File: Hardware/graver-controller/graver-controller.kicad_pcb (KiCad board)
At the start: 2 copper layers, 95 x 70 mm, 117 parts, among them J101 Power in 2p, J201 Handpiece pads 1x4, J301 USB-C, J302 SWD, J401 LCD pads 1x7, J402 Pedal pads 1x4, J403 Encoder pads 1x4, Q101 DMP6023LE, Q201 IRLR3410, Q202 SI2309CDS, Q203 BSS123, SW301 BOOT0, SW302 RESET, U101 LM5164DDAR, U102 AP2112K-3.3, U201 UCC27517DBVR, U202 TLV9062IDR, U301 STM32F411CEU6, U302 USBLC6-2SC6, U401 PESD5V0S2BT, Y301 25MHz 10pF

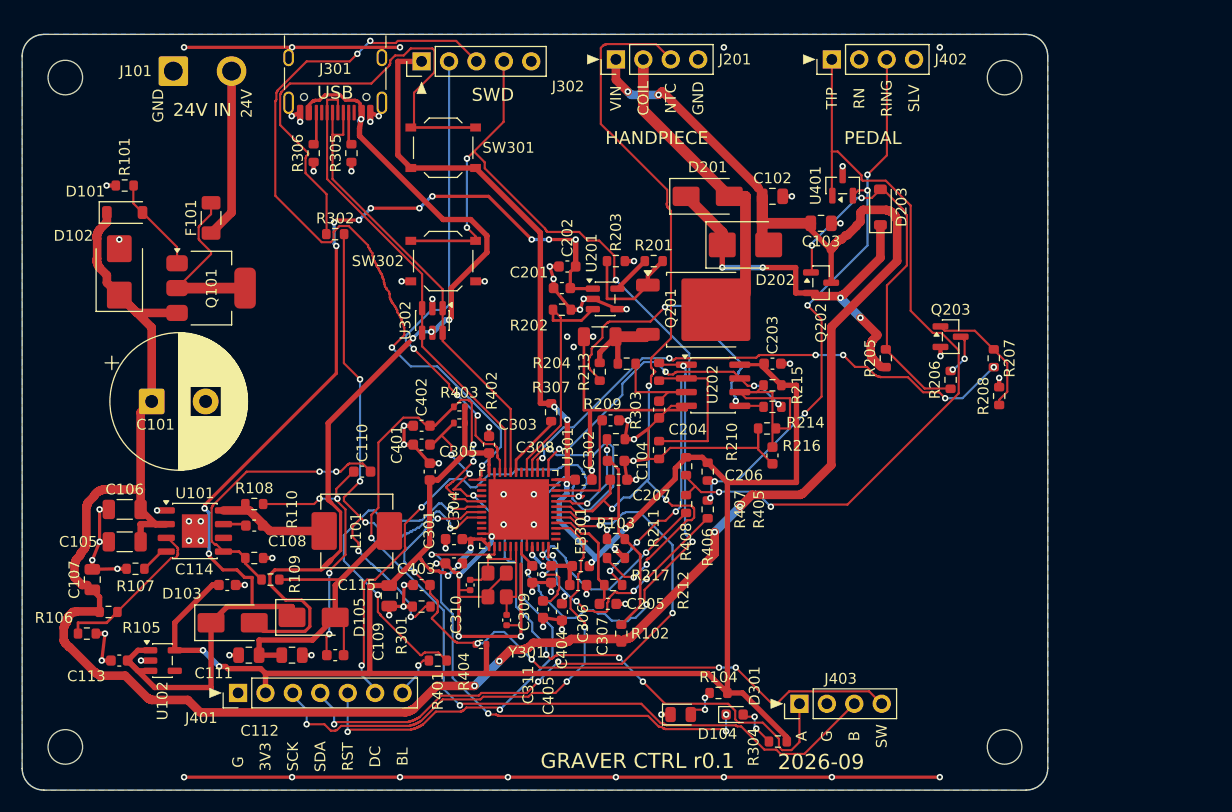
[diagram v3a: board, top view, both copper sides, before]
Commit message: pcb: ADR 0005 stage 1 - 4-layer board, rules, placement with pcbkit
New board from the netlist with pcbkit mkboard: 85 x 60 mm (the ADR 0005
ceiling), JLC04161H-7628 stackup, In1 = GND plane, In2 = +3V3 plane. Net
classes and board rules per ADR 0005 Decision 3 in the .kicad_pro, width
floors in the .kicad_dru, all of it driven from pcbkit.toml.

tools/pcb5/place.py places all 117 parts in bands (power left, MCU centre,
driver right, pad rows on the rear and front edges), adds the M3 and crystal
keepouts, an L-shaped 25 x 20 mm ADR 0004 boost reserve at the front left,
the inner plane zones and the QFN EP vias, and prints the ADR 0003 distance
checks (all PASS). USB-C mouth flush with the rear edge, straight 10.6 mm
run to the MCU for the 0.25/0.15 pair.

tools/pcb5/check.py is the acceptance checker for the component spec
(via and width sets, per-net floors, inner layers track-free, In1 under
USB/crystal/analog, USB skew and vias, placement distances, DRC summary);
postroute.py, render.sh and build.sh are the rest of the pipeline.
tools/pcb/ (ADR 0003 pipeline) stays reachable at tag pcb-pre-pcbkit.
output/pcb/*.png and drc.rpt are no longer ignored (ADR 0005 acceptance).
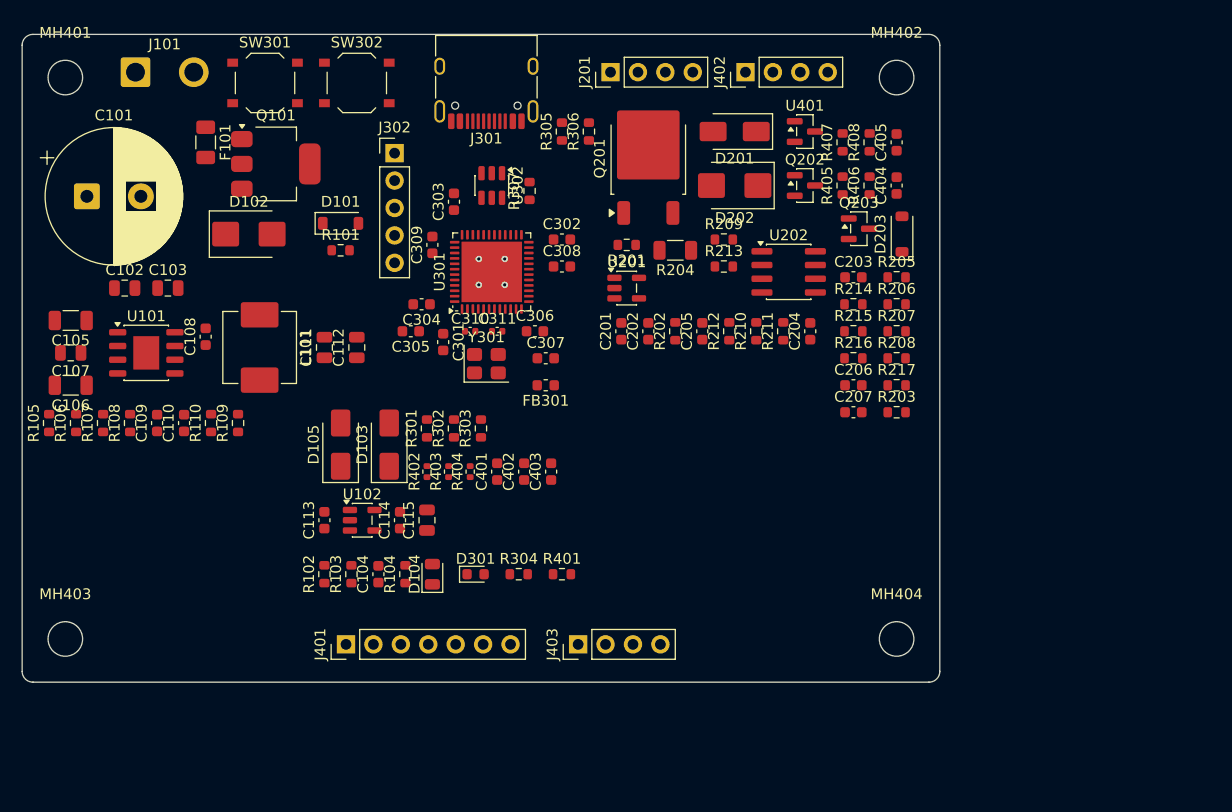
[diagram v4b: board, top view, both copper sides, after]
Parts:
- moved MH403 87.6 mm to (54.0, 106.0)
- moved MH404 77.6 mm to (131.0, 106.0)
- moved C103 60.8 mm to (63.5, 73.5)
- moved C102 60.6 mm to (59.5, 73.5)
- moved C405 54.3 mm to (131.0, 60.0), turned to 90 degrees
- moved C404 50.2 mm to (131.0, 64.0), turned to 90 degrees
- moved R408 37.6 mm to (128.5, 60.0), turned to 90 degrees
- moved R406 33.5 mm to (128.5, 64.0), turned to 90 degrees
- moved R407 33.3 mm to (126.0, 60.0), turned to 90 degrees
- moved C309 31.9 mm to (88.0, 69.5), turned to 90 degrees
- moved R104 31.0 mm to (85.5, 100.0), turned to 90 degrees
- moved R217 30.5 mm to (131.0, 82.5), turned to 0 degrees
- moved R203 29.5 mm to (131.0, 85.0)
- moved C111 29.3 mm to (78.0, 79.0), turned to 90 degrees
- moved R405 29.3 mm to (126.0, 64.0), turned to 90 degrees
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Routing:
- net GND: track 254.5 -> 0.00 mm, vias 85 -> 4
- net +3V3: track 249.7 -> 0.00 mm, vias 11 -> 0
- net VIN: track 222.3 -> 0.00 mm, vias 6 -> 0
- net +5V: track 103.9 -> 0.00 mm, vias 11 -> 0
- net NRST: track 95.0 -> 0.00 mm, vias 6 -> 0
- net ENC_B: track 91.9 -> 0.00 mm, vias 4 -> 0
- net NTC: track 81.2 -> 0.00 mm, vias 5 -> 0
- net VBUS: track 79.2 -> 0.00 mm, vias 4 -> 0
- net SWCLK: track 74.1 -> 0.00 mm, vias 4 -> 0
- net Net-(J402-Pin_1): track 73.3 -> 0.00 mm, vias 2 -> 0
- net LCD_RST: track 65.9 -> 0.00 mm, vias 3 -> 0
- net ENC_SW: track 62.8 -> 0.00 mm, vias 6 -> 0
- net ENC_A: track 62.4 -> 0.00 mm, vias 6 -> 0
- net LCD_MOSI: track 57.2 -> 0.00 mm, vias 5 -> 0
- net Net-(U301-BOOT0): track 56.6 -> 0.00 mm, vias 6 -> 0
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- added copper zone on In2.Cu, net +3V3
- added copper zone on In1.Cu, net GND
- removed copper zone on B.Cu, net GND
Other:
- board size 95 x 70 mm -> 85 x 60 mm
- copper layers 2 -> 4
- board text removed: "2026-09"
- board text removed: "24V"
- board text removed: "24V IN"
- board text removed: "3V3"
- board text removed: "A"
- board text removed: "B"
- board text removed: "BL"
- board text removed: "COIL"
- board text removed: "DC"
- board text removed: "G"
- board text removed: "GND"
- board text removed: "GRAVER CTRL r0.1"
- board text removed: "HANDPIECE"
- board text removed: "NTC"
- board text removed: "PEDAL"
- board text removed: "RING"
- board text removed: "RN"
- board text removed: "RST"
- board text removed: "SCK"
- board text removed: "SDA"
- board text removed: "SLV"
- board text removed: "SW"
- board text removed: "SWD"
- board text removed: "TIP"
- board text removed: "USB"
- board text removed: "VIN"

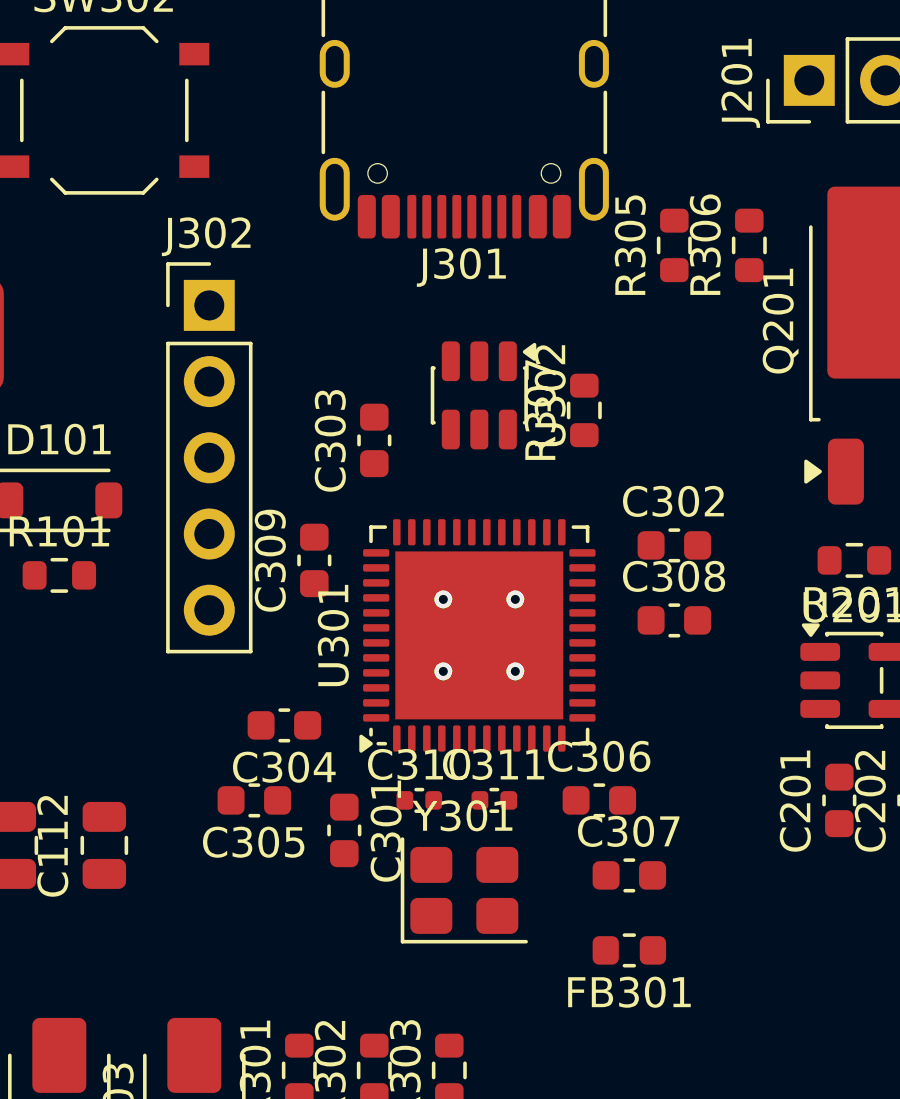
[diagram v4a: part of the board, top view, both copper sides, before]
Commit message: pcb: ADR 0005 stage 2 - scripted USB pair and crystal, router settings
tools/pcb5/handroute.py draws the USB pair J301 -> USBLC6 -> MCU on F.Cu at
0.25/0.15 with no vias: pad stubs above (D+) and below (D-) the connector
row so neither crosses the other, an orthogonal detour sized from the two
leg lengths so the skew is 0.000 mm, and the crystal's OSC tracks through
the load caps. The copper sits in group 'hand', which krt-route now keeps.

Router clearance 0.15 (the Default class), USB class clearance 0.15, the
crystal keepout now blocks B.Cu tracks only so the crystal's own tracks and
its GND vias are allowed. check.py reads the ADR distances pad edge to pad
edge and parses the kicad-cli parity line. widen.py (new) lifts router
stubs to their class width where DRC allows.
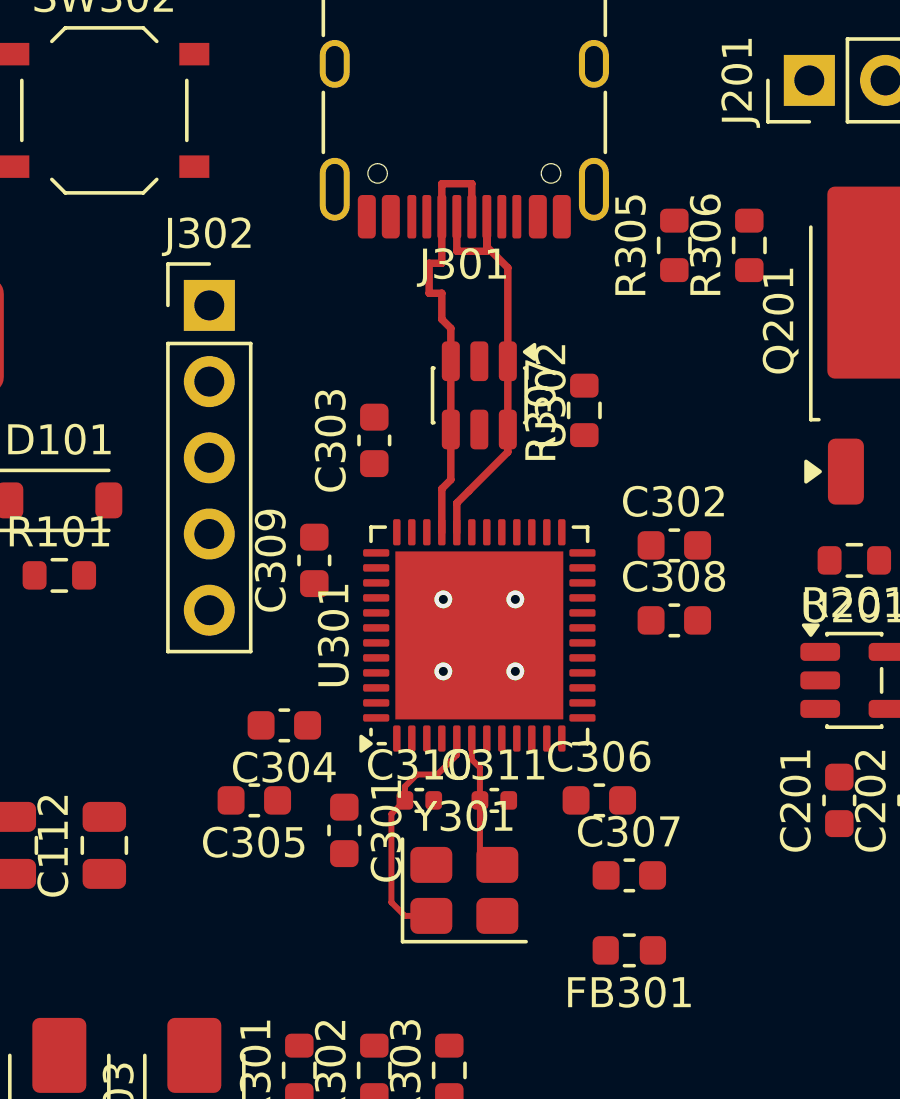
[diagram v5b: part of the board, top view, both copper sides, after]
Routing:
- net /MCU/USB_DP: track 0.00 -> 14.8 mm
- net /MCU/USB_DM: track 0.00 -> 14.8 mm
- net /MCU/OSC_IN: track 0.00 -> 8.28 mm
- net /MCU/OSC_OUT: track 0.00 -> 4.90 mm

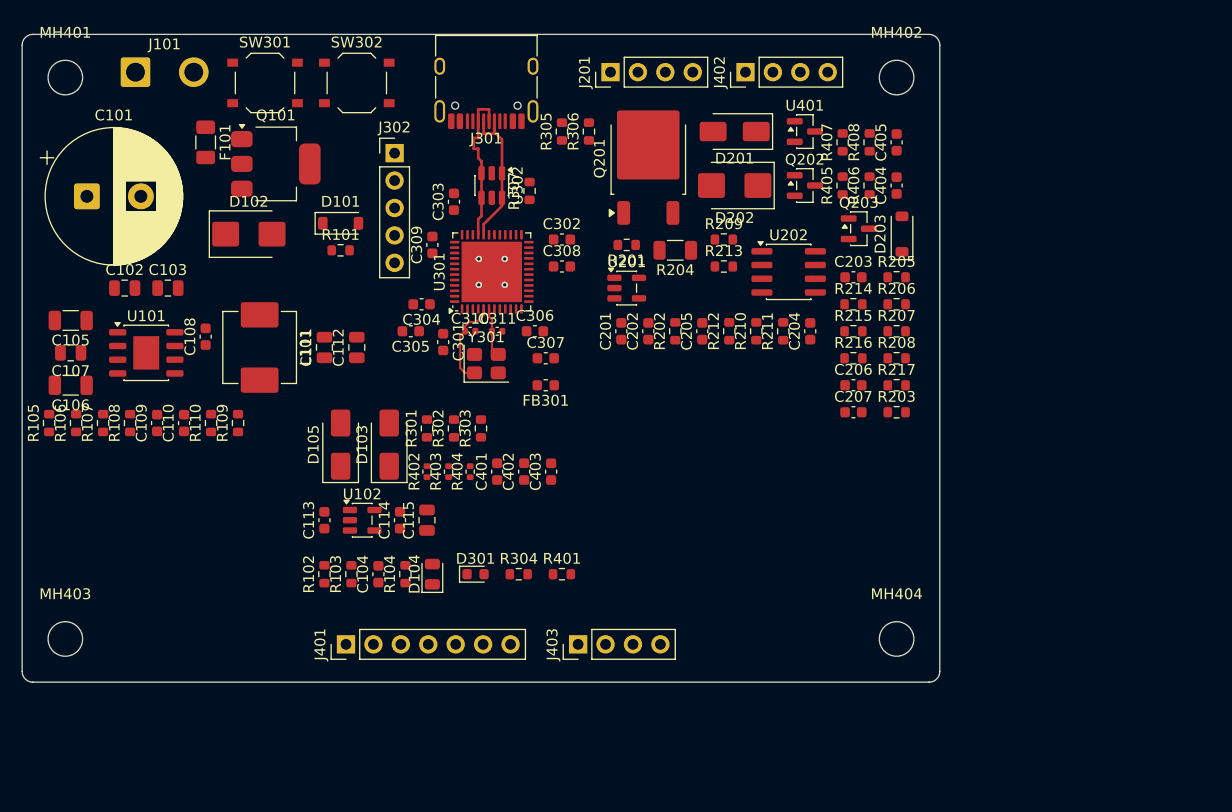
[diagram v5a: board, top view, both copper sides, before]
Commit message: pcb: ADR 0005 stage 3 (WIP) - routed board, pours, silk, labels; 31 opens
KRT routed everything except 10 single-pin nets on the QFN's left and
bottom sides (DECAY_SLOW, ENC_B, LCD_BL/DC/MOSI/RST, LED_STAT, NRST, PB2,
VIN_SENSE); the USB pair and crystal hand routes survived the run. DRC on
this board: 0 parity, 31 unconnected, 151 errors (93 track_width necks
below the .kicad_dru floors, 27 stitching vias inside the boost reserve
from a gndpour bug now fixed in pcbkit, 31 opens). Not finished: see the
ADR 'As built' section and the session handoff.
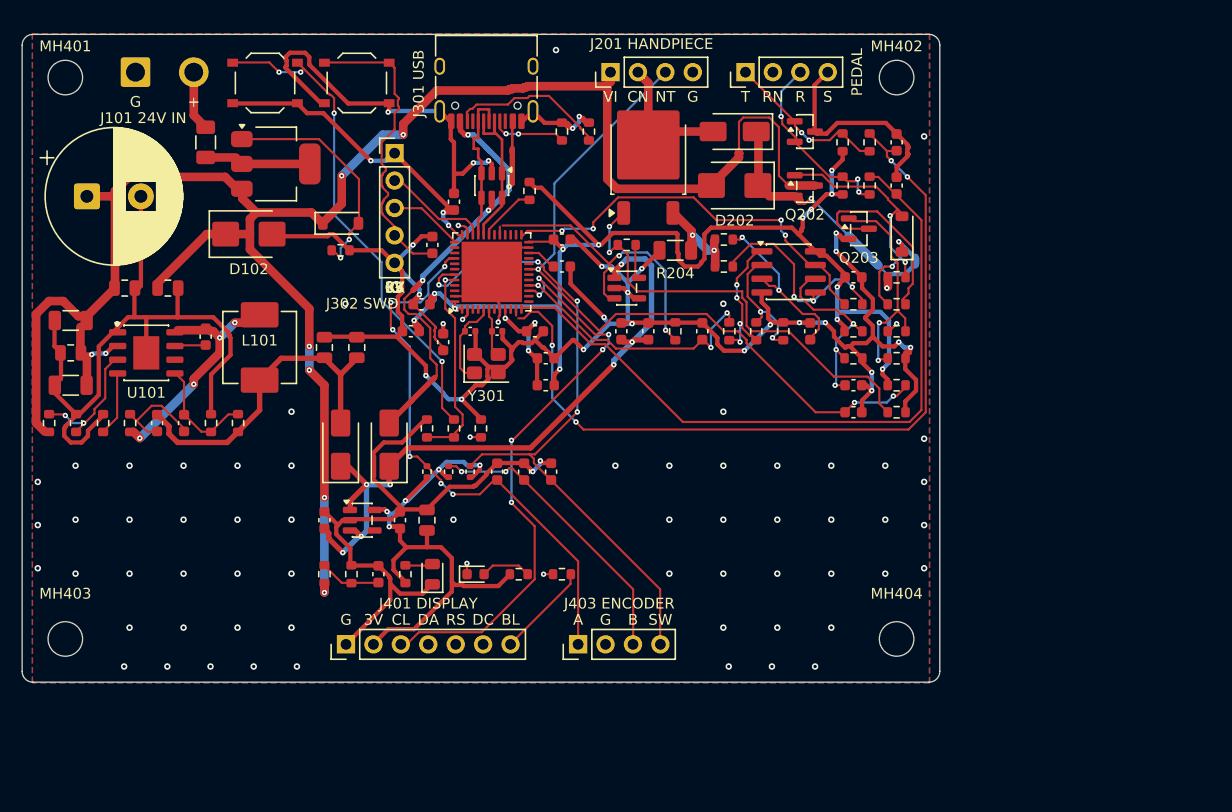
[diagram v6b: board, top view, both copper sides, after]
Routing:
- net GND: track 0.00 -> 382.7 mm, vias 4 -> 90
- net +3V3: track 0.00 -> 190.8 mm, vias 0 -> 22
- net VIN: track 0.00 -> 184.7 mm, vias 0 -> 8
- net PEDAL_TIP: track 0.00 -> 76.2 mm, vias 0 -> 4
- net PEDAL_RING: track 0.00 -> 65.9 mm
- net NTC: track 0.00 -> 65.8 mm, vias 0 -> 3
- net +5V: track 0.00 -> 62.4 mm, vias 0 -> 7
- net ENC_SW: track 0.00 -> 62.1 mm, vias 0 -> 4
- net LCD_SCK: track 0.00 -> 53.1 mm, vias 0 -> 6
- net ENC_A: track 0.00 -> 51.1 mm, vias 0 -> 6
- net Net-(R302-Pad2): track 0.00 -> 46.2 mm, vias 0 -> 4
- net VBUS: track 0.00 -> 45.1 mm, vias 0 -> 4
- net Net-(Q201-G): track 0.00 -> 40.6 mm, vias 0 -> 2
- net OC_TRIP: track 0.00 -> 36.6 mm, vias 0 -> 4
- net Net-(D105-A): track 0.00 -> 30.6 mm
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- added copper zone on B.Cu, net GND
- added copper zone on F.Cu, net GND
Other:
- board text added: "+"
- board text added: "3V"
- board text added: "A"
- board text added: "B"
- board text added: "BL"
- board text added: "CK"
- board text added: "CL"
- board text added: "CN"
- board text added: "DA"
- board text added: "DC"
- board text added: "G"
- board text added: "IO"
- board text added: "J101 24V IN"
- board text added: "J201 HANDPIECE"
- board text added: "J301 USB"
- board text added: "J302 SWD"
- board text added: "J401 DISPLAY"
- board text added: "J403 ENCODER"
- board text added: "NT"
- board text added: "PEDAL"
- board text added: "R"
- board text added: "RN"
- board text added: "RS"
- board text added: "S"
- board text added: "SW"
- board text added: "T"
- board text added: "VI"
